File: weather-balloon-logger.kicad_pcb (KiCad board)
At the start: 2 copper layers, 80 x 70 mm, 22 parts, among them J1 Conn_01x02, J2 Conn_01x11, J3 SMA, J4 SMA, J5 Conn_01x02, J6 VHF, J7 HF, Q1 AO3400A, SW1 SPDT, U1 PCF8574T

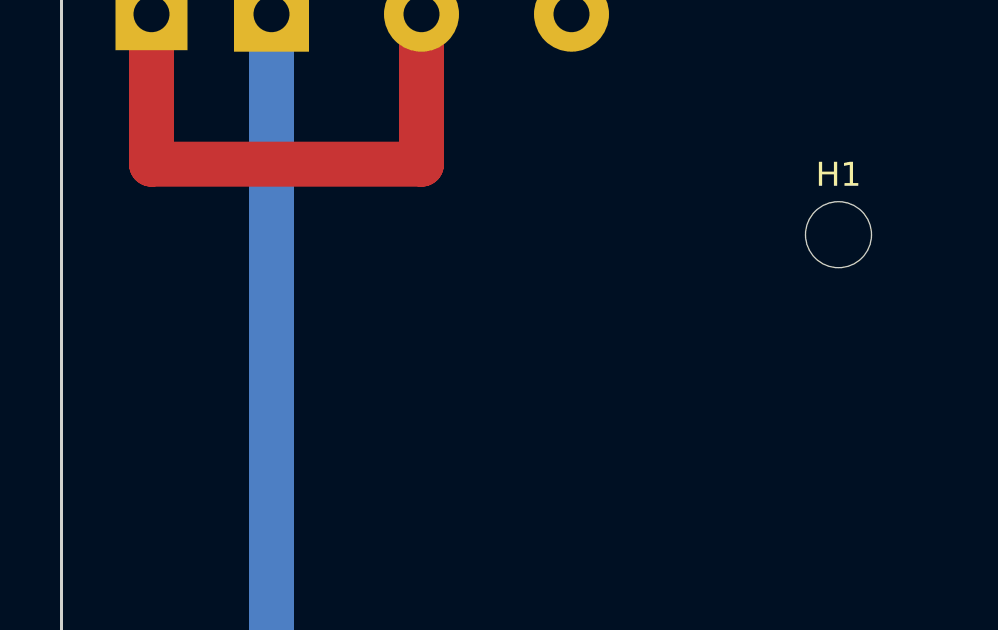
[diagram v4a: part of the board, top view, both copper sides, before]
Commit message: copperhead: Add front-silkscreen (F.SilkS) board label text reading 'JAVAS Logger' in a clear, readable area that does not overlap any component, pad, trace, mounting hole (H1-H4), the 32.77 x 54.80 mm module zone, or the >=5 mm SMA keepouts. Use a standard silkscreen text height of about 1.5-2 mm, horizontal and right-reading (upright). A good open area is the left-center of the board. Update docs/LAYOUT.md to note the label, then re-run DRC and keep it clean.
Added the horizontal, right-reading `JAVAS Logger` label to F.SilkS at (114.5, 118.0) mm with 1.8 mm height and 0.30 mm stroke. The label is documented in docs/LAYOUT.md and remains clear of components, pads, traces, H1-H4, the LightAPRS-W module zone, and both SMA keepouts. Updated the changelog and recorded the placement decision. PCB SVG export succeeded; ERC, DRC, and drift checks are clean.

Verification: ERC clean, DRC clean
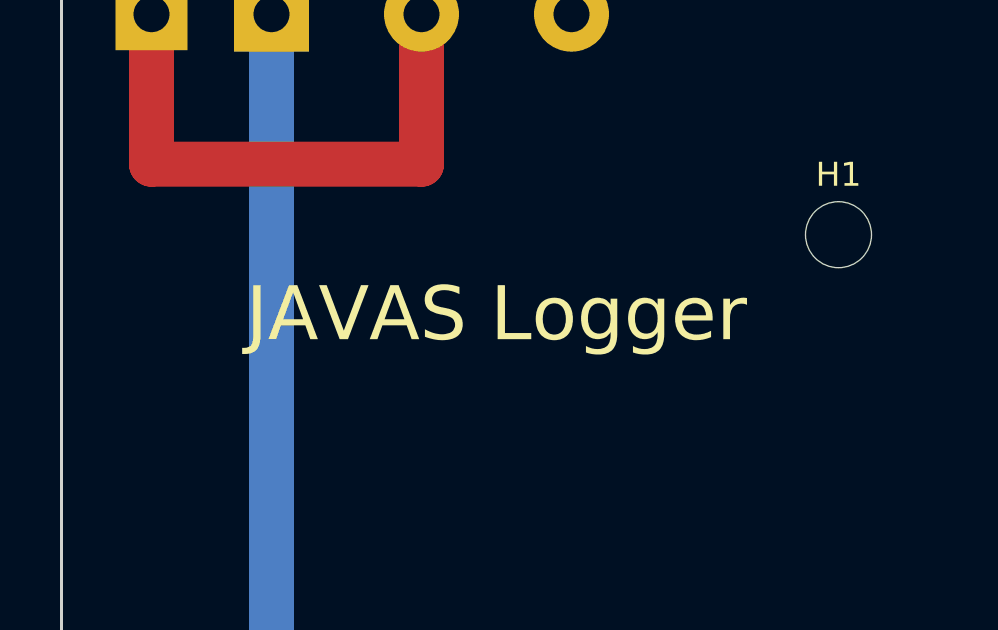
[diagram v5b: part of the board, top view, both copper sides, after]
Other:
- board text added: "JAVAS Logger"
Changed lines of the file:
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@@
 		(effects (font (size 0.8 0.8) (thickness 0.12)))
+	)
+	(gr_text "JAVAS Logger" (at 114.5 118) (layer "F.SilkS")
+		(effects (font (size 1.8 1.8) (thickness 0.3)))
 	)
 	(footprint "CopperheadDraft_MountingHole_2.2mm"

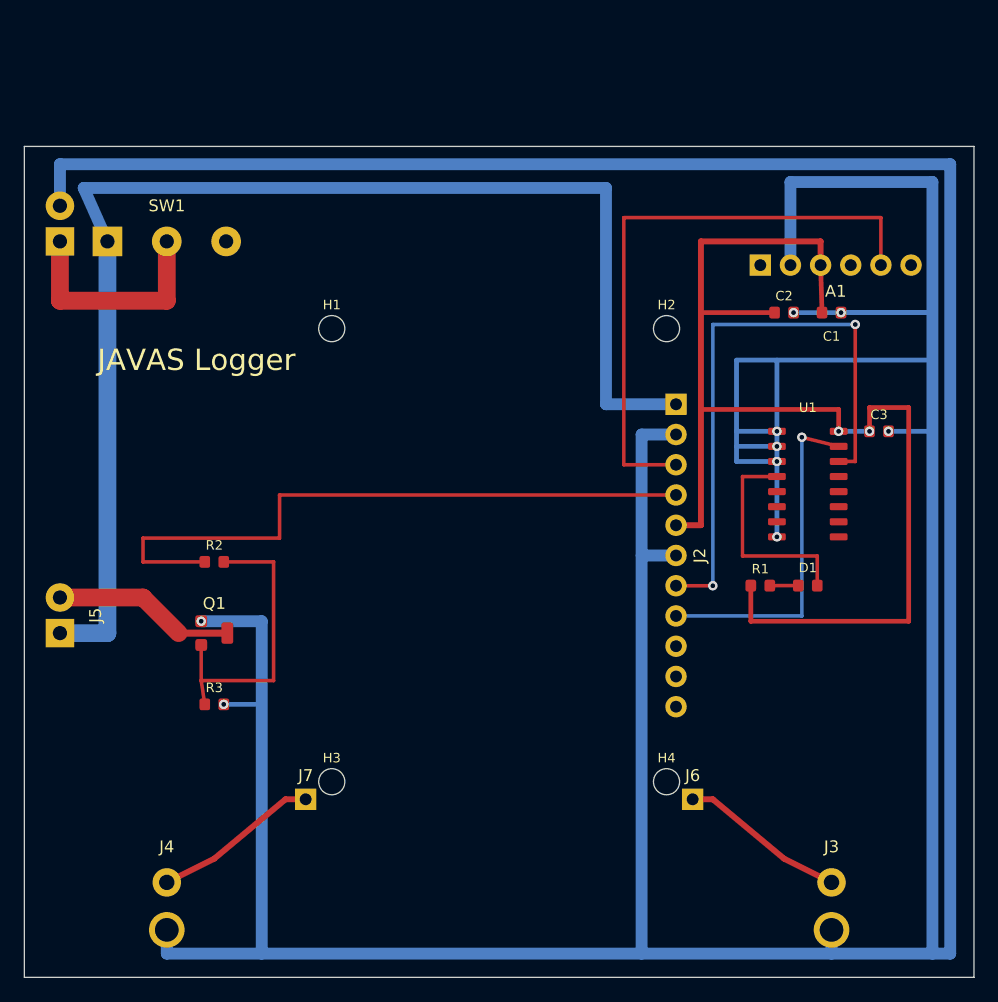
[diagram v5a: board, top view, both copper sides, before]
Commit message: fix(pcb): repair real footprint routing
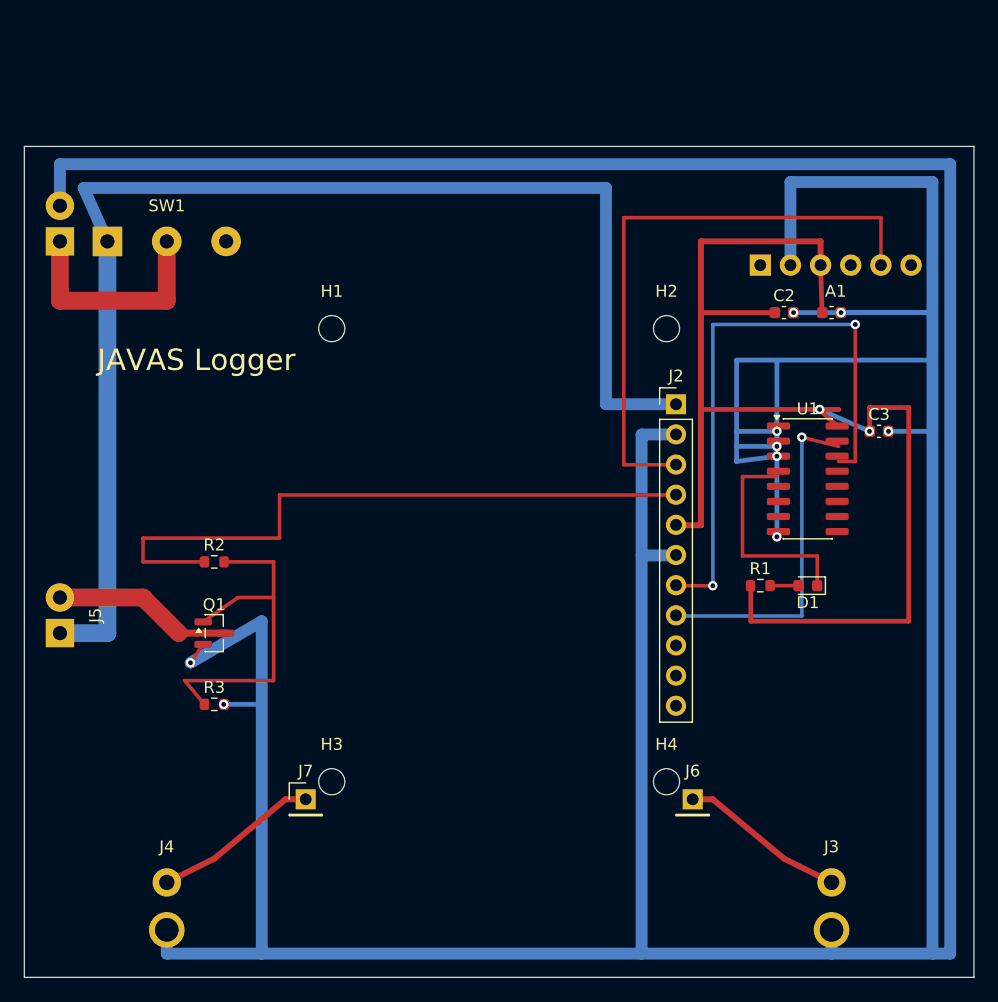
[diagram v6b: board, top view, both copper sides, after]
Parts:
- C1, C2, C3: footprint CopperheadDraft_C_0603_1608Metric -> C_0603_1608Metric
- D1: footprint CopperheadDraft_LED_0603_1608Metric -> LED_0603_1608Metric
- H1, H2, H3, H4: footprint CopperheadDraft_MountingHole_2.2mm -> MountingHole_2.2mm_M2
- J2: footprint CopperheadDraft_PinHeader_1x11_P2.54mm_Vertical -> PinHeader_1x11_P2.54mm_Vertical
- J6, J7: footprint CopperheadDraft_PinHeader_1x01_P2.54mm_Vertical -> PinHeader_1x01_P2.54mm_Vertical
- Q1: footprint CopperheadDraft_SOT-23 -> SOT-23
- R1, R2, R3: footprint CopperheadDraft_R_0603_1608Metric -> R_0603_1608Metric
- U1: footprint CopperheadDraft_SOIC-16_3.9x9.9mm_P1.27mm -> SOIC-16_3.9x9.9mm_P1.27mm
- turned J2 to 0 degrees
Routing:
- net CUTDOWN_GATE: track 25.3 -> 30.9 mm
- net 3V3: track 103.9 -> 107.7 mm
- net GND: track 458.0 -> 461.8 mm

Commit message: copperhead: Power connector pass only. J1, J5, and SW1 now contain their exact real footprints: Connector_JST:JST_PH_S2B-PH-K_1x02_P2.00mm_Horizontal, Connector_JST:JST_XH_S2B-XH-A_1x02_P2.50mm_Horizontal, and WeatherBalloon:SW_CK_7101SYZQE. SW1 is the requested C&K 7101SYZQE with direct-solder plated slots; keep its library identity and pad geometry.\n\nRepair this batch in the smallest manufacturable change:\n- Keep the board outline and every footprint except J1, J5, and SW1 fixed.\n- You may move and rotate only J1, J5, and SW1 so their real bodies/courtyards do not overlap, remain fully inside the board, and their mating/actuation directions remain accessible from board edges for hand assembly.\n- Preserve net intent: SW1 pad 2 is PACK_IN common, pad 1 is switched PACK_SW, and pad 3 is intentionally no-connect. Never connect pad 3.\n- Reroute only PACK_IN, PACK_SW, GND, and CUTDOWN_OUT as locally necessary; remove stale track segments beneath the real switch/connector bodies.\n- Maintain existing current-capable track widths for the battery and cutdown paths.\n- Resolve all new courtyard, edge, silkscreen, solder-mask, short, and connectivity findings without global DRC suppression. Reference-text or nonfunctional silk may move/hide.\n- Preserve the six already documented and exact vendor-module exclusions in weather-balloon-logger.kicad_pro.\n- Update docs/FOOTPRINT_AUDIT.md with final J1/J5/SW1 locations/orientations and hand-assembly accessibility.\n- Run kicad-cli DRC and Copperhead checks. Commit this bounded pass only if normal DRC has zero violations and zero unconnected items.
Completed the bounded power-connector pass. J1 remains at (103,108) 90° and J5 at (103,141) 90° with their real rotated courtyards fully inside the board and side-entry mating access at the left edge. SW1 retains the exact WeatherBalloon:SW_CK_7101SYZQE footprint and plated-slot pad geometry, moves only to (114,108) 0°, keeps pad 2=PACK_IN, pad 1=PACK_SW, and pad 3 intentionally u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
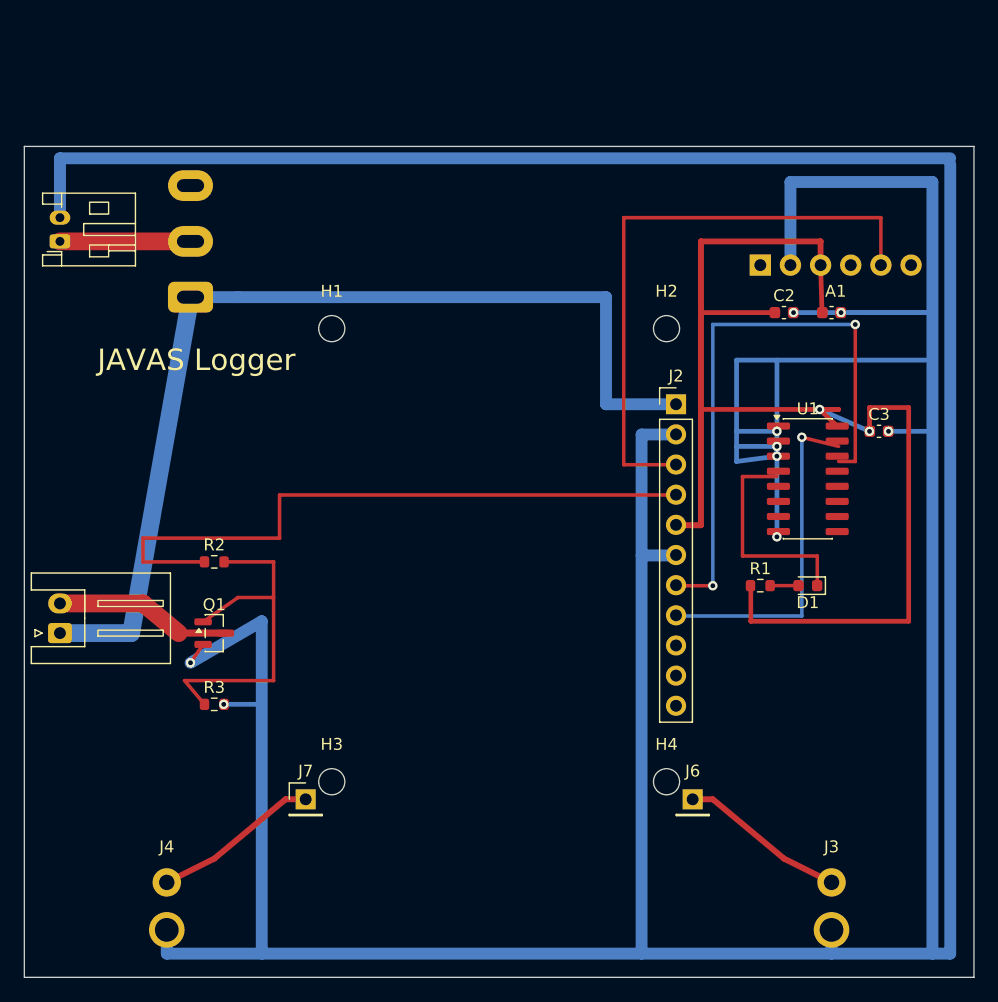
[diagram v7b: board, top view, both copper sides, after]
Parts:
- J1: footprint CopperheadDraft_Molex_Micro-Fit_3.0_43650-0200_1x02_P3.00mm_Horizontal -> JST_PH_S2B-PH-K_1x02_P2.00mm_Horizontal
- J5: footprint CopperheadDraft_Molex_Micro-Fit_3.0_43650-0200_1x02_P3.00mm_Horizontal -> JST_XH_S2B-XH-A_1x02_P2.50mm_Horizontal
- SW1: footprint CopperheadDraft_SW_CK_7101MD9CQE -> SW_CK_7101SYZQE
- moved SW1 2.00 mm to (114.0, 108.0)
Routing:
- net PACK_SW: track 110.0 -> 84.7 mm
- net PACK_IN: track 19.0 -> 11.0 mm
- net GND: track 461.8 -> 463.3 mm

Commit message: copperhead: OpenLog mechanical pass only. A1 now contains the exact project footprint WeatherBalloon:SparkFun_OpenLog_DEV-13712_Carrier with the official 15.24 x 19.05 mm module body/courtyard and solder-down header. The real body currently extends above the draft board outline, and only two stale routes plus two A1 edge-silk findings remain.\n\nMake the smallest coherent OpenLog layout change:\n- Keep the exact A1 footprint identity, pad geometry, top-side installation, and direct-solder assembly.\n- Keep the LightAPRS module interface J2/J6/J7/H1-H4 and its 32.77 x 54.80 mm reserved body coordinates fixed.\n- Keep all footprints fixed except A1, C1, and C2. You may move/rotate only those three to create a practical OpenLog cluster outside the LightAPRS body zone.\n- Enlarge the board outline only as much as needed to fully contain A1's courtyard and allow practical access to the OpenLog microSD card and header for home assembly. Prefer extending the top/right edges rather than disturbing the fixed module and bottom RF layout.\n- Keep A1 pin order BLK through GRN and preserve nets: pad 2 GND, pad 3 3V3, pad 5 UART_TX; unused module pins remain intentionally unconnected as captured.\n- Reroute only A1/C1/C2-related GND, 3V3, and UART_TX copper. Remove stale route ends and keep bypass capacitors reasonably close to A1's supply pins.\n- Keep every other footprint and route unchanged except an unavoidable ground/power trunk extension.\n- Preserve the six exact documented LightAPRS interface exclusions and do not add global DRC suppression.\n- Resolve all DRC/connectivity/silkscreen/edge findings and update docs/LAYOUT.md and docs/FOOTPRINT_AUDIT.md with the final outline and A1/C1/C2 coordinates plus access rationale.\n- Run normal kicad-cli DRC and Copperhead checks. Commit only with zero normal DRC violations and zero unconnected items.
Completed the bounded OpenLog mechanical pass. A1 retains the exact WeatherBalloon:SparkFun_OpenLog_DEV-13712_Carrier footprint, top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
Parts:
- A1: footprint CopperheadDraft_PinSocket_1x06_P2.54mm_Vertical -> SparkFun_OpenLog_DEV-13712_Carrier
- moved A1 9.00 mm to (171.0, 110.0)
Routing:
- net UART_TX: track 50.9 -> 39.6 mm
- net 3V3: track 107.7 -> 111.7 mm
- net GND: track 463.3 -> 459.4 mm
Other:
- board size 80 x 70 mm -> 80 x 78.5 mm
